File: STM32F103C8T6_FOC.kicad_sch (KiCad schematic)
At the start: 5 parts

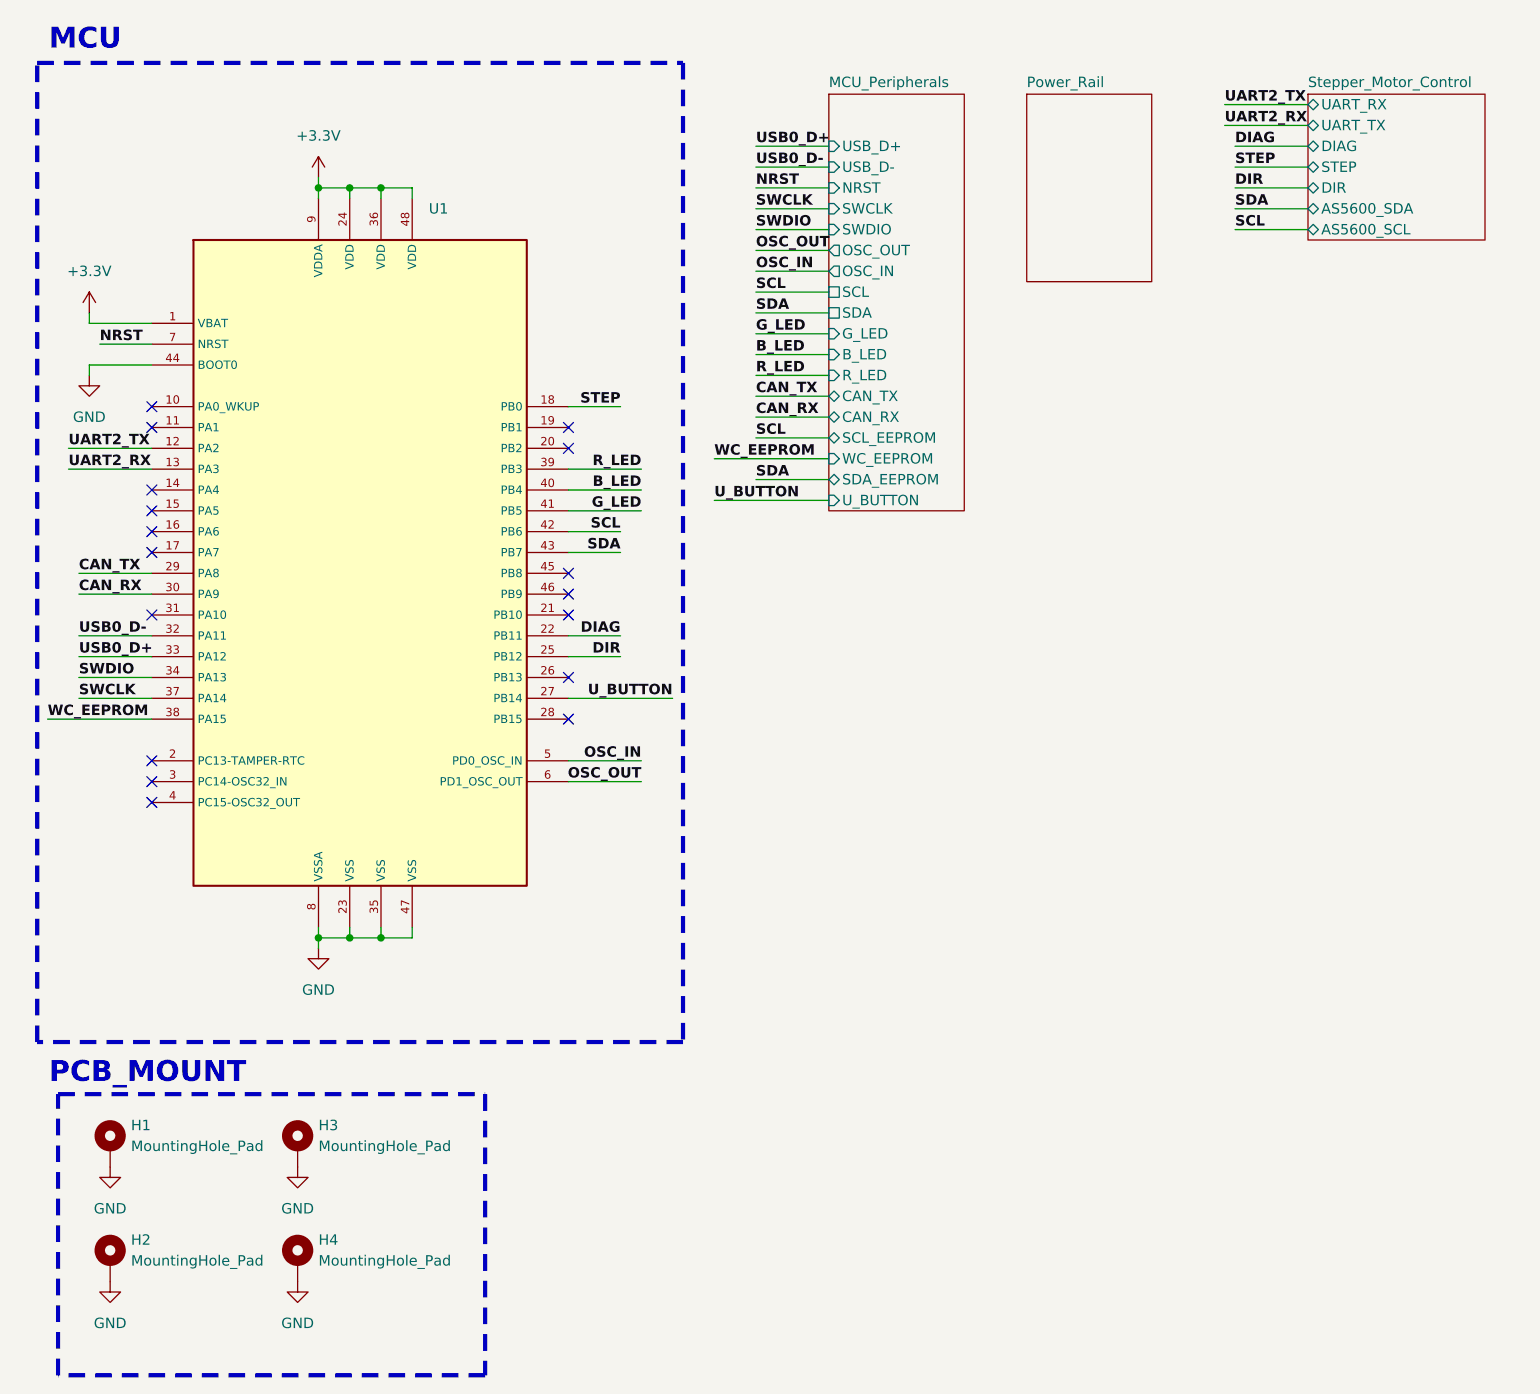
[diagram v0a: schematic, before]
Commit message: Schematic check, Text adjustment & QoL changes
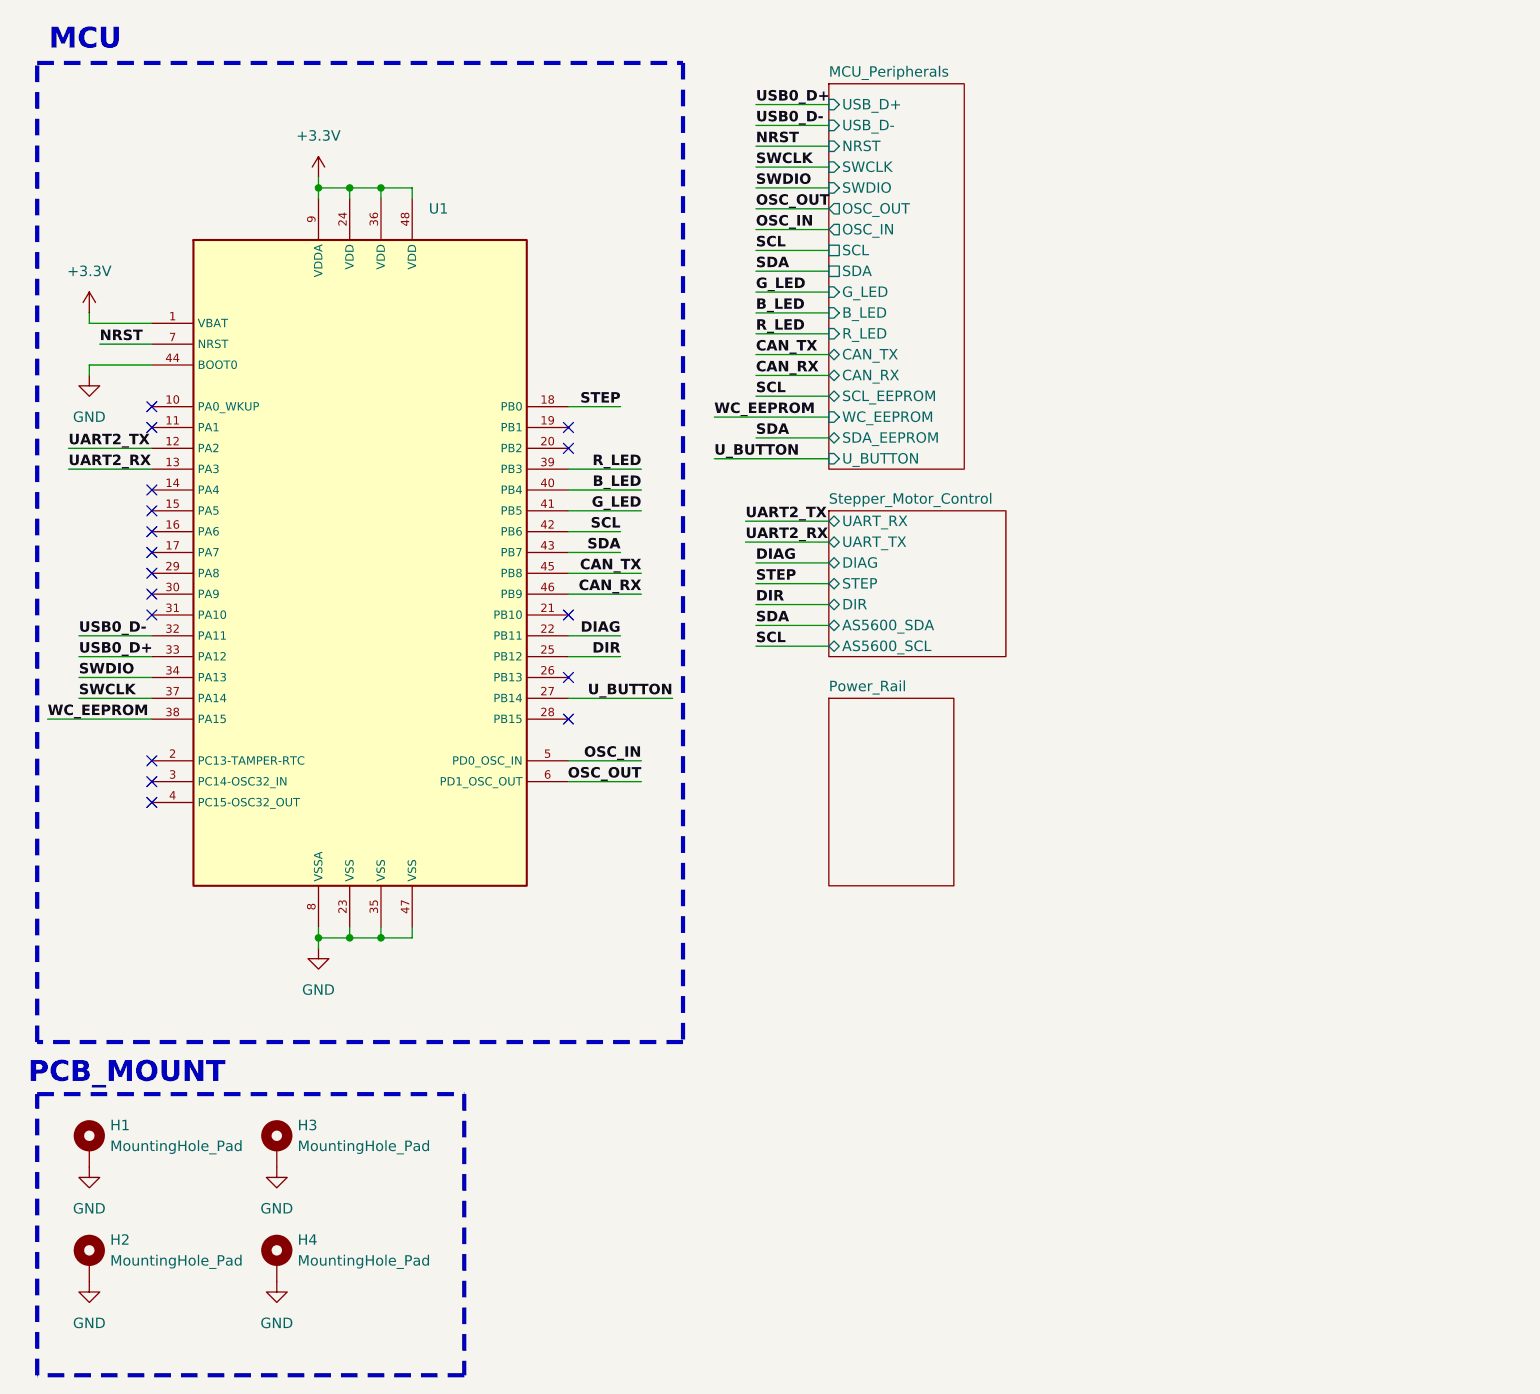
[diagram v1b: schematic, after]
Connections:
- net CAN_RX: now also U1.46 (PB9); no longer U1.30 (PA9)
- net CAN_TX: now also U1.45 (PB8); no longer U1.29 (PA8)
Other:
- moved on the sheet: H1, H2, H3, H4
